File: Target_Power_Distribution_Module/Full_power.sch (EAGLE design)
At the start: 13 parts, among them Q1 NFET, Q2 PFET, Q3 NFET, Q4 PFET

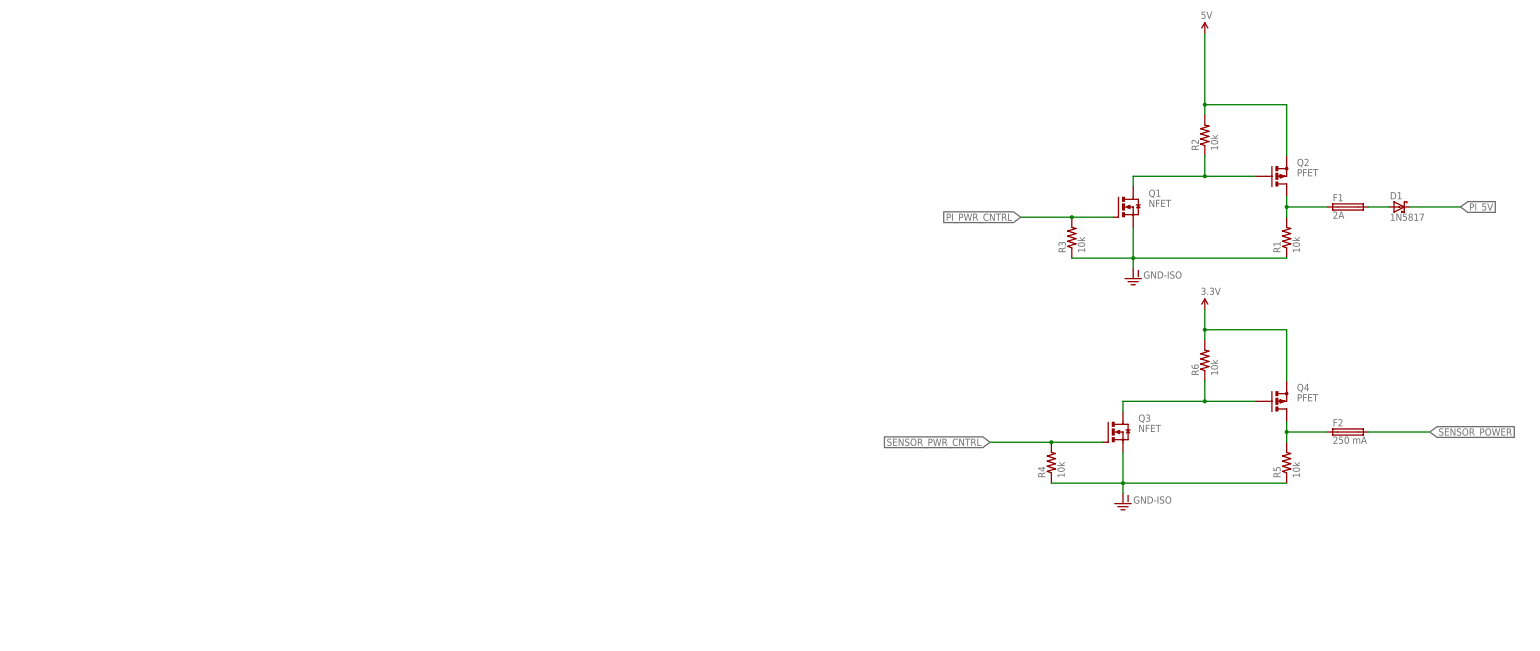
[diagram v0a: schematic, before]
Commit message: Created full power schematic
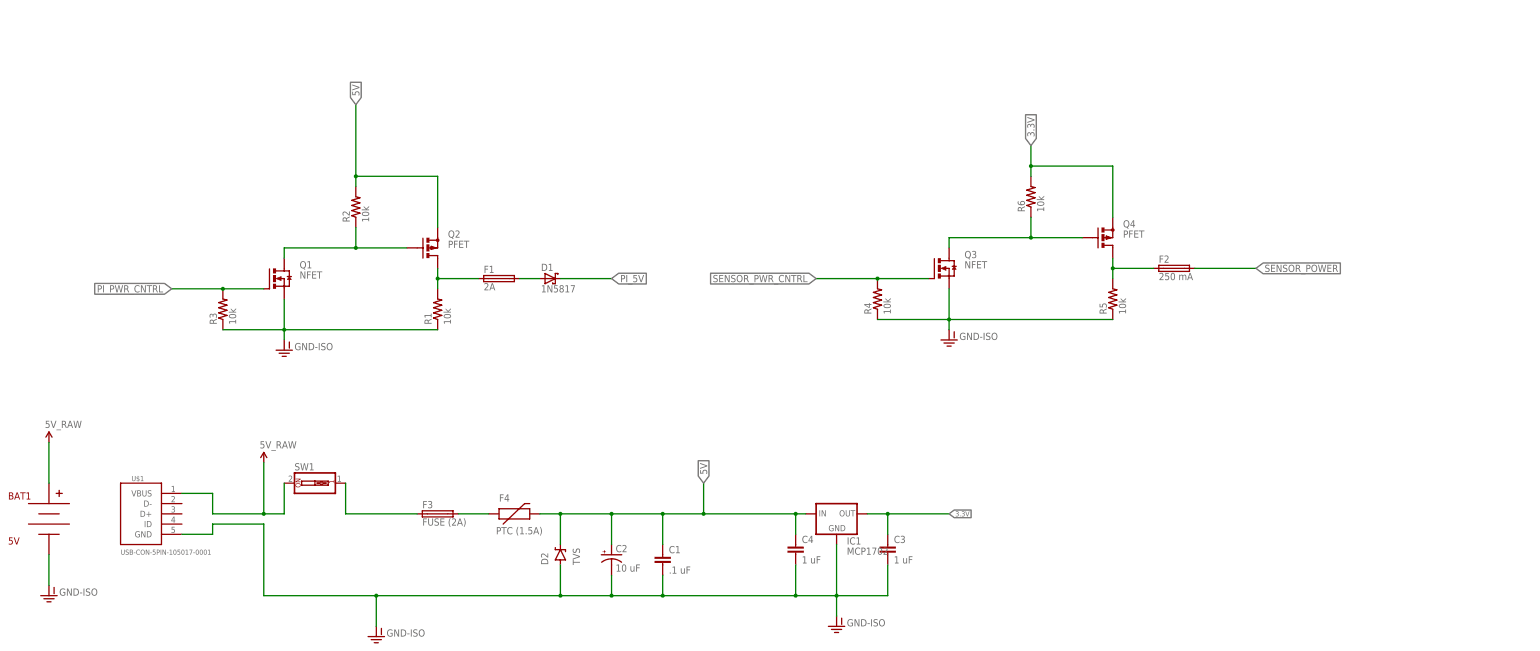
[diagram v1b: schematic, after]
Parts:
- added BAT1: 5V, SparkFun-Connectors:BC9VPC
- added C1: .1 uF, SparkFun-Capacitors:CAP1206
- added C2: 10 uF, SparkFun-Passives:CAP_POLPTH2
- added C3, C4: 1 uF, SparkFun-Capacitors:CAPPTH
- added D2: TVS, SparkFun-DiscreteSemi:DIODE-ZENERPTH
- added F3: FUSE (2A), fuse:FUSE1821
- added F4: PTC (1.5A), SparkFun-PowerIC:PTCPTH
- added IC1: MCP1702, adafruit:MCP1700TRI
- added SW1: (no value), special:SW_DIP-1
- added U$1: USB-CON-5PIN-105017-0001, GeekAmmo:USB-CON-5PIN-105017-0001
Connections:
- new net 5V_RAW: BAT1.V+, SW1.2, U$1.VBUS
- new net 5V_SWITCH: F3.1, SW1.1
- new net N$7: F3.2, F4.1
- net 3.3V: now also C3.1, IC1.OUT
- net 5V: now also C1.1, C2.+, C4.1, D2.C, F4.2, IC1.IN
- net GND-ISO: now also BAT1.V-, C1.2, C2.-, C3.2, C4.2, D2.A, IC1.GND, U$1.GND
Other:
- moved on the sheet: D1, F1, F2, Q1, Q2, Q3, Q4, R1, R2, R3, R4, R5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

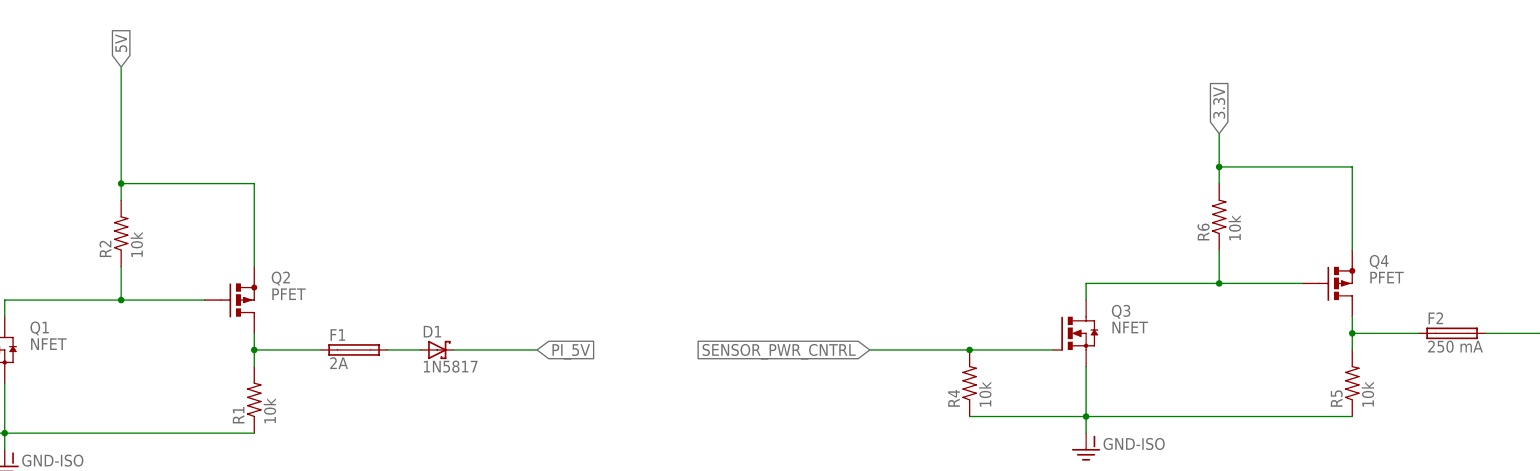
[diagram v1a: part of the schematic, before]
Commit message: Added backup switches in case power control fails
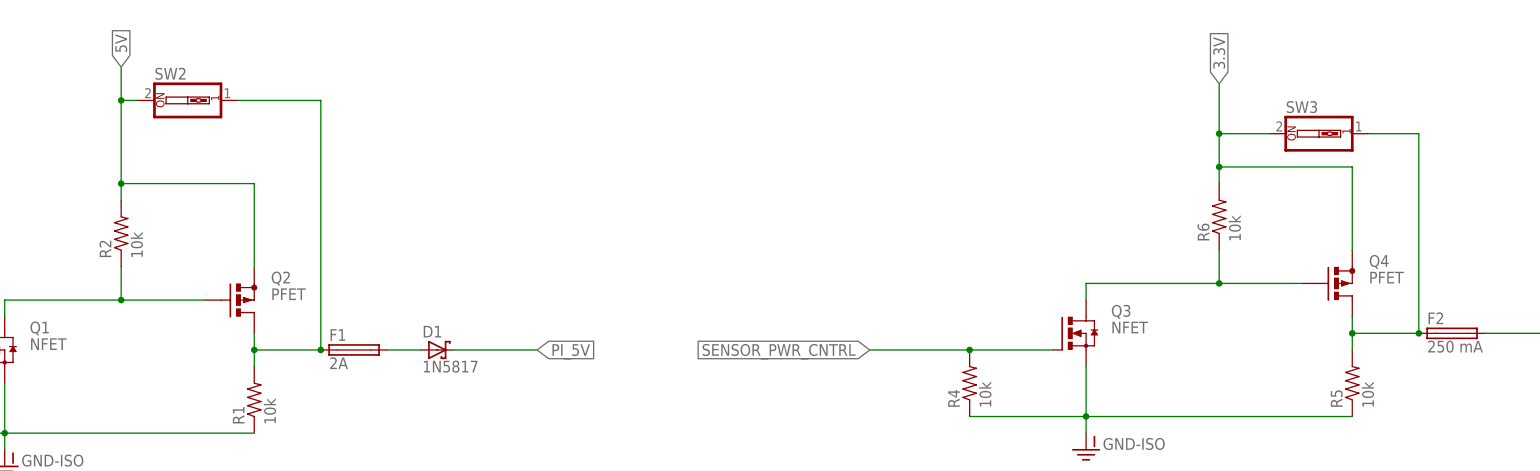
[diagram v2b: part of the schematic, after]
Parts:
- added SW2, SW3: (no value), special:SW_DIP-1
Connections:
- net 3.3V: now also SW3.2
- net 5V: now also SW2.2
- net N$4: now also SW2.1
- net N$6: now also SW3.1
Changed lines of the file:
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@@
 <part name="C3" library="SparkFun-Capacitors" deviceset="CAP" device="PTH" value="1 uF"/>
 <part name="C4" library="SparkFun-Capacitors" deviceset="CAP" device="PTH" value="1 uF"/>
+<part name="SW2" library="special" deviceset="SW_DIP-1" device=""/>
+<part name="SW3" library="special" deviceset="SW_DIP-1" device=""/>
 </parts>
 <sheets>
@@
 <instance part="C3" gate="G$1" x="-30.48" y="-38.1"/>
 <instance part="C4" gate="G$1" x="-53.34" y="-38.1"/>
+<instance part="SW2" gate="G$1" x="-152.4" y="68.58"/>
+<instance part="SW3" gate="G$1" x="20.32" y="63.5"/>
 </instances>
 <busses>
@@
 <wire x1="-142.24" y1="30.48" x2="-132.08" y2="30.48" width="0.1524" layer="91"/>
 <junction x="-142.24" y="30.48"/>
+<pinref part="SW2" gate="G$1" pin="1"/>
+<wire x1="-144.78" y1="68.58" x2="-132.08" y2="68.58" width="0.1524" layer="91"/>
+<wire x1="-132.08" y1="68.58" x2="-132.08" y2="30.48" width="0.1524" layer="91"/>
+<junction x="-132.08" y="30.48"/>
 </segment>
 </net>
@@
 <wire x1="5.08" y1="58.42" x2="5.08" y2="63.5" width="0.1524" layer="91"/>
 <junction x="5.08" y="58.42"/>
-<label x="5.08" y="63.5" size="1.778" layer="95" rot="R90" xref="yes"/>
+<label x="5.08" y="71.12" size="1.778" layer="95" rot="R90" xref="yes"/>
+<pinref part="SW3" gate="G$1" pin="2"/>
+<wire x1="5.08" y1="63.5" x2="5.08" y2="71.12" width="0.1524" layer="91"/>
+<wire x1="12.7" y1="63.5" x2="5.08" y2="63.5" width="0.1524" layer="91"/>
+<junction x="5.08" y="63.5"/>
 </segment>
 <segment>
@@
 <wire x1="-142.24" y1="43.18" x2="-142.24" y2="55.88" width="0.1524" layer="91"/>
 <wire x1="-142.24" y1="55.88" x2="-162.56" y2="55.88" width="0.1524" layer="91"/>
-<wire x1="-162.56" y1="55.88" x2="-162.56" y2="73.66" width="0.1524" layer="91"/>
+<wire x1="-162.56" y1="55.88" x2="-162.56" y2="68.58" width="0.1524" layer="91"/>
 <pinref part="R2" gate="G$1" pin="2"/>
+<wire x1="-162.56" y1="68.58" x2="-162.56" y2="73.66" width="0.1524" layer="91"/>
 <wire x1="-162.56" y1="55.88" x2="-162.56" y2="53.34" width="0.1524" layer="91"/>
 <junction x="-162.56" y="55.88"/>
 <label x="-162.56" y="73.66" size="1.778" layer="95" rot="R90" xref="yes"/>
+<pinref part="SW2" gate="G$1" pin="2"/>
+<wire x1="-162.56" y1="68.58" x2="-160.02" y2="68.58" width="0.1524" layer="91"/>
+<junction x="-162.56" y="68.58"/>
 </segment>
 <segment>
@@
 <wire x1="25.4" y1="33.02" x2="35.56" y2="33.02" width="0.1524" layer="91"/>
 <junction x="25.4" y="33.02"/>
-</segment>
-</net>
+<pinref part="SW3" gate="G$1" pin="1"/>
+<wire x1="27.94" y1="63.5" x2="35.56" y2="63.5" width="0.1524" layer="91"/>
+<wire x1="35.56" y1="63.5" x2="35.56" y2="33.02" width="0.1524" layer="91"/>
+<junction x="35.56" y="33.02"/>
+</segment>
+</net>

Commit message: Started on brd
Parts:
- F3: value FUSE (2A) -> FUSE (3.5A); device fuse:FUSE1821 -> fuse:PICOFUSE
- Q1, Q3: device transistor-power:IRF3704 -> User-Submitted:MOSFET-PCHANNELFQP27P06
- Q2, Q4: device adafruit:PFETBS250 -> User-Submitted:MOSFET-PCHANNELFQP27P06
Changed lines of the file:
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@@
 </classes>
 <parts>
-<part name="Q1" library="transistor-power" deviceset="IRF3704" device="" value="NFET"/>
-<part name="Q2" library="adafruit" deviceset="PFET" device="BS250" value="PFET"/>
+<part name="Q1" library="User-Submitted" deviceset="MOSFET-PCHANNEL" device="FQP27P06" value="NFET"/>
+<part name="Q2" library="User-Submitted" deviceset="MOSFET-PCHANNEL" device="FQP27P06" value="PFET"/>
 <part name="GND-ISO1" library="SparkFun-Aesthetics" deviceset="GND-ISO" device=""/>
 <part name="R1" library="SparkFun-Resistors" deviceset="RESISTOR" device="1206" value="10k"/>
@@
 <part name="D1" library="adafruit" deviceset="SCHOTTKY-DIODE" device="CB429-15" value="1N5817"/>
 <part name="F1" library="fuse" deviceset="FUSE" device="PICOFUSE" value="2A"/>
-<part name="Q3" library="transistor-power" deviceset="IRF3704" device="" value="NFET"/>
-<part name="Q4" library="adafruit" deviceset="PFET" device="BS250" value="PFET"/>
+<part name="Q3" library="User-Submitted" deviceset="MOSFET-PCHANNEL" device="FQP27P06" value="NFET"/>
+<part name="Q4" library="User-Submitted" deviceset="MOSFET-PCHANNEL" device="FQP27P06" value="PFET"/>
 <part name="F2" library="fuse" deviceset="FUSE" device="PICOFUSE" value="250 mA"/>
 <part name="R4" library="SparkFun-Resistors" deviceset="RESISTOR" device="1206" value="10k"/>
@@
 <part name="U$1" library="GeekAmmo" deviceset="USB-CON-5PIN" device="-105017-0001"/>
 <part name="D2" library="SparkFun-DiscreteSemi" deviceset="DIODE-ZENER" device="PTH" value="TVS"/>
-<part name="F3" library="fuse" deviceset="FUSE" device="1821" value="FUSE (2A)"/>
+<part name="F3" library="fuse" deviceset="PICOFUSE" device="" value="FUSE (3.5A)"/>
 <part name="F4" library="SparkFun-PowerIC" deviceset="PTC" device="PTH" value="PTC (1.5A)"/>
 <part name="C1" library="SparkFun-Capacitors" deviceset="CAP" device="1206" value=".1 uF"/>
@@
 </plain>
 <instances>
-<instance part="Q1" gate="G$1" x="-182.88" y="30.48"/>
-<instance part="Q2" gate="1" x="-144.78" y="38.1"/>
+<instance part="Q1" gate="G$1" x="-180.34" y="33.02"/>
+<instance part="Q2" gate="G$1" x="-142.24" y="38.1" rot="MR180"/>
 <instance part="GND-ISO1" gate="G$1" x="-180.34" y="12.7"/>
 <instance part="R1" gate="G$1" x="-142.24" y="22.86" rot="R90"/>
@@
 <instance part="D1" gate="G$1" x="-114.3" y="30.48"/>
 <instance part="F1" gate="G$1" x="-127" y="30.48"/>
-<instance part="Q3" gate="G$1" x="-17.78" y="33.02"/>
-<instance part="Q4" gate="1" x="22.86" y="40.64"/>
+<instance part="Q3" gate="G$1" x="-15.24" y="30.48"/>
+<instance part="Q4" gate="G$1" x="25.4" y="40.64" rot="MR180"/>
 <instance part="F2" gate="G$1" x="40.64" y="33.02"/>
 <instance part="R4" gate="G$1" x="-33.02" y="25.4" rot="R90"/>
@@
 <attribute name="VALUE" x="-106.9086" y="-40.64" size="1.778" layer="96" rot="R90"/>
 </instance>
-<instance part="F3" gate="G$1" x="-142.24" y="-27.94"/>
+<instance part="F3" gate="1" x="-142.24" y="-27.94"/>
 <instance part="F4" gate="G$1" x="-124.46" y="-27.94"/>
 <instance part="C1" gate="G$1" x="-86.36" y="-40.64"/>
@@
 <pinref part="Q1" gate="G$1" pin="S"/>
 <pinref part="GND-ISO1" gate="G$1" pin="GND-ISO"/>
-<wire x1="-180.34" y1="25.4" x2="-180.34" y2="17.78" width="0.1524" layer="91"/>
+<wire x1="-180.34" y1="27.94" x2="-180.34" y2="17.78" width="0.1524" layer="91"/>
 <pinref part="R3" gate="G$1" pin="1"/>
 <wire x1="-180.34" y1="17.78" x2="-180.34" y2="15.24" width="0.1524" layer="91"/>
@@
 <junction x="-15.24" y="20.32"/>
 <pinref part="Q3" gate="G$1" pin="S"/>
-<wire x1="-15.24" y1="27.94" x2="-15.24" y2="20.32" width="0.1524" layer="91"/>
+<wire x1="-15.24" y1="25.4" x2="-15.24" y2="20.32" width="0.1524" layer="91"/>
 </segment>
 <segment>
@@
 <segment>
 <pinref part="Q1" gate="G$1" pin="D"/>
-<wire x1="-180.34" y1="35.56" x2="-180.34" y2="38.1" width="0.1524" layer="91"/>
-<pinref part="Q2" gate="1" pin="G"/>
+<pinref part="Q2" gate="G$1" pin="G"/>
 <wire x1="-180.34" y1="38.1" x2="-162.56" y2="38.1" width="0.1524" layer="91"/>
 <pinref part="R2" gate="G$1" pin="1"/>
@@
 <segment>
 <pinref part="R3" gate="G$1" pin="2"/>
+<wire x1="-195.58" y1="27.94" x2="-208.28" y2="27.94" width="0.1524" layer="91"/>
+<label x="-208.28" y="27.94" size="1.778" layer="95" rot="R180" xref="yes"/>
+<wire x1="-195.58" y1="27.94" x2="-195.58" y2="33.02" width="0.1524" layer="91"/>
+<junction x="-195.58" y="27.94"/>
 <pinref part="Q1" gate="G$1" pin="G"/>
-<wire x1="-195.58" y1="27.94" x2="-185.42" y2="27.94" width="0.1524" layer="91"/>
-<wire x1="-195.58" y1="27.94" x2="-208.28" y2="27.94" width="0.1524" layer="91"/>
-<junction x="-195.58" y="27.94"/>
-<label x="-208.28" y="27.94" size="1.778" layer="95" rot="R180" xref="yes"/>
+<wire x1="-195.58" y1="33.02" x2="-187.96" y2="33.02" width="0.1524" layer="91"/>
 </segment>
 </net>
@@
 <segment>
 <pinref part="R1" gate="G$1" pin="2"/>
-<pinref part="Q2" gate="1" pin="D"/>
+<pinref part="Q2" gate="G$1" pin="D"/>
 <wire x1="-142.24" y1="27.94" x2="-142.24" y2="30.48" width="0.1524" layer="91"/>
 <pinref part="F1" gate="G$1" pin="1"/>
@@
 <net name="N$1" class="0">
 <segment>
-<pinref part="Q4" gate="1" pin="G"/>
+<pinref part="Q4" gate="G$1" pin="G"/>
 <pinref part="R6" gate="G$1" pin="1"/>
 <wire x1="17.78" y1="40.64" x2="5.08" y2="40.64" width="0.1524" layer="91"/>
 <wire x1="5.08" y1="40.64" x2="5.08" y2="45.72" width="0.1524" layer="91"/>
 <pinref part="Q3" gate="G$1" pin="D"/>
-<wire x1="-15.24" y1="38.1" x2="-15.24" y2="40.64" width="0.1524" layer="91"/>
+<wire x1="-15.24" y1="35.56" x2="-15.24" y2="40.64" width="0.1524" layer="91"/>
 <wire x1="-15.24" y1="40.64" x2="5.08" y2="40.64" width="0.1524" layer="91"/>
 <junction x="5.08" y="40.64"/>
@@
 <net name="3.3V" class="0">
 <segment>
-<pinref part="Q4" gate="1" pin="S"/>
+<pinref part="Q4" gate="G$1" pin="S"/>
 <wire x1="25.4" y1="45.72" x2="25.4" y2="58.42" width="0.1524" layer="91"/>
 <wire x1="25.4" y1="58.42" x2="5.08" y2="58.42" width="0.1524" layer="91"/>
@@
 <net name="5V" class="0">
 <segment>
-<pinref part="Q2" gate="1" pin="S"/>
+<pinref part="Q2" gate="G$1" pin="S"/>
 <wire x1="-142.24" y1="43.18" x2="-142.24" y2="55.88" width="0.1524" layer="91"/>
 <wire x1="-142.24" y1="55.88" x2="-162.56" y2="55.88" width="0.1524" layer="91"/>
@@
 <pinref part="R4" gate="G$1" pin="2"/>
 <pinref part="Q3" gate="G$1" pin="G"/>
-<wire x1="-33.02" y1="30.48" x2="-20.32" y2="30.48" width="0.1524" layer="91"/>
+<wire x1="-33.02" y1="30.48" x2="-22.86" y2="30.48" width="0.1524" layer="91"/>
 <wire x1="-33.02" y1="30.48" x2="-48.26" y2="30.48" width="0.1524" layer="91"/>
 <junction x="-33.02" y="30.48"/>
@@
 <net name="N$6" class="0">
 <segment>
-<pinref part="Q4" gate="1" pin="D"/>
+<pinref part="Q4" gate="G$1" pin="D"/>
 <pinref part="R5" gate="G$1" pin="2"/>
 <wire x1="25.4" y1="35.56" x2="25.4" y2="33.02" width="0.1524" layer="91"/>
@@
 <net name="N$7" class="0">
 <segment>
-<pinref part="F3" gate="G$1" pin="2"/>
+<pinref part="F3" gate="1" pin="2"/>
 <pinref part="F4" gate="G$1" pin="1"/>
 <wire x1="-137.16" y1="-27.94" x2="-129.54" y2="-27.94" width="0.1524" layer="91"/>
@@
 <net name="5V_SWITCH" class="0">
 <segment>
-<pinref part="F3" gate="G$1" pin="1"/>
+<pinref part="F3" gate="1" pin="1"/>
 <wire x1="-147.32" y1="-27.94" x2="-165.1" y2="-27.94" width="0.1524" layer="91"/>
 <pinref part="SW1" gate="G$1" pin="1"/>
